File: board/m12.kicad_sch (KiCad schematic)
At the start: 1 part, among them J2 M12D-04PFFP-SF8001

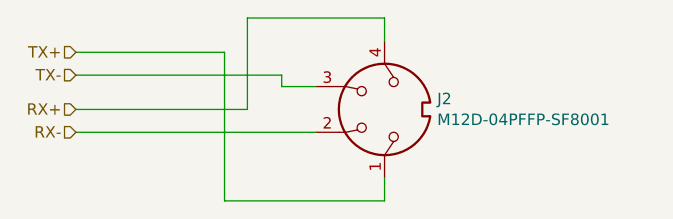
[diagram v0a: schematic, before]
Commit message: changed subsheet name
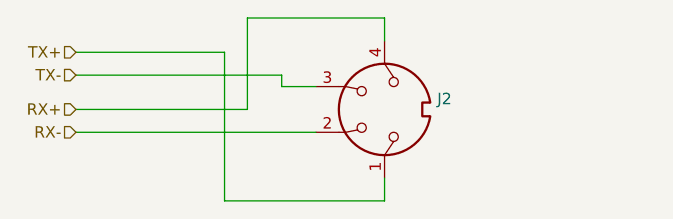
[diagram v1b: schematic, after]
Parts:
- J2: value M12D-04PFFP-SF8001 -> (none); footprint b095:M12D -> (none)
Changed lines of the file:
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@@
       (effects (font (size 1.27 1.27)) (justify right))
     )
-    (property "Value" "M12D-04PFFP-SF8001" (id 1) (at 127.762 88.773 90)
+    (property "Value" "" (id 1) (at 127.762 88.773 90)
       (effects (font (size 1.27 1.27)) (justify right))
     )
-    (property "Footprint" "b095:M12D" (id 2) (at 121.92 87.63 0)
+    (property "Footprint" "" (id 2) (at 121.92 87.63 0)
       (effects (font (size 1.27 1.27)) hide)
     )

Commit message: updated put_on_edge submodule
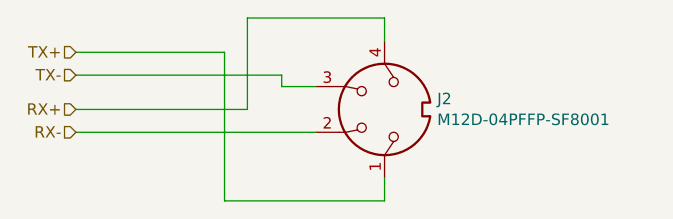
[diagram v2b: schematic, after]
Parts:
- J2: value (none) -> M12D-04PFFP-SF8001; footprint (none) -> b095:M12D
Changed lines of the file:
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@@
       (effects (font (size 1.27 1.27)) (justify right))
     )
-    (property "Value" "" (id 1) (at 127.762 88.773 90)
+    (property "Value" "M12D-04PFFP-SF8001" (id 1) (at 127.762 88.773 90)
       (effects (font (size 1.27 1.27)) (justify right))
     )
-    (property "Footprint" "" (id 2) (at 121.92 87.63 0)
+    (property "Footprint" "b095:M12D" (id 2) (at 121.92 87.63 0)
       (effects (font (size 1.27 1.27)) hide)
     )
